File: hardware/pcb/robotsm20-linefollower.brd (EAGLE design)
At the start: 230 x 100 mm, 139 parts, among them Q5 BSS138LT3G, Q6 BSS138LT3G, Q7 BSS138LT3G, Q8 BSS138LT3G, SW1 CTS_219-4LPST, U1 STM32F405RG

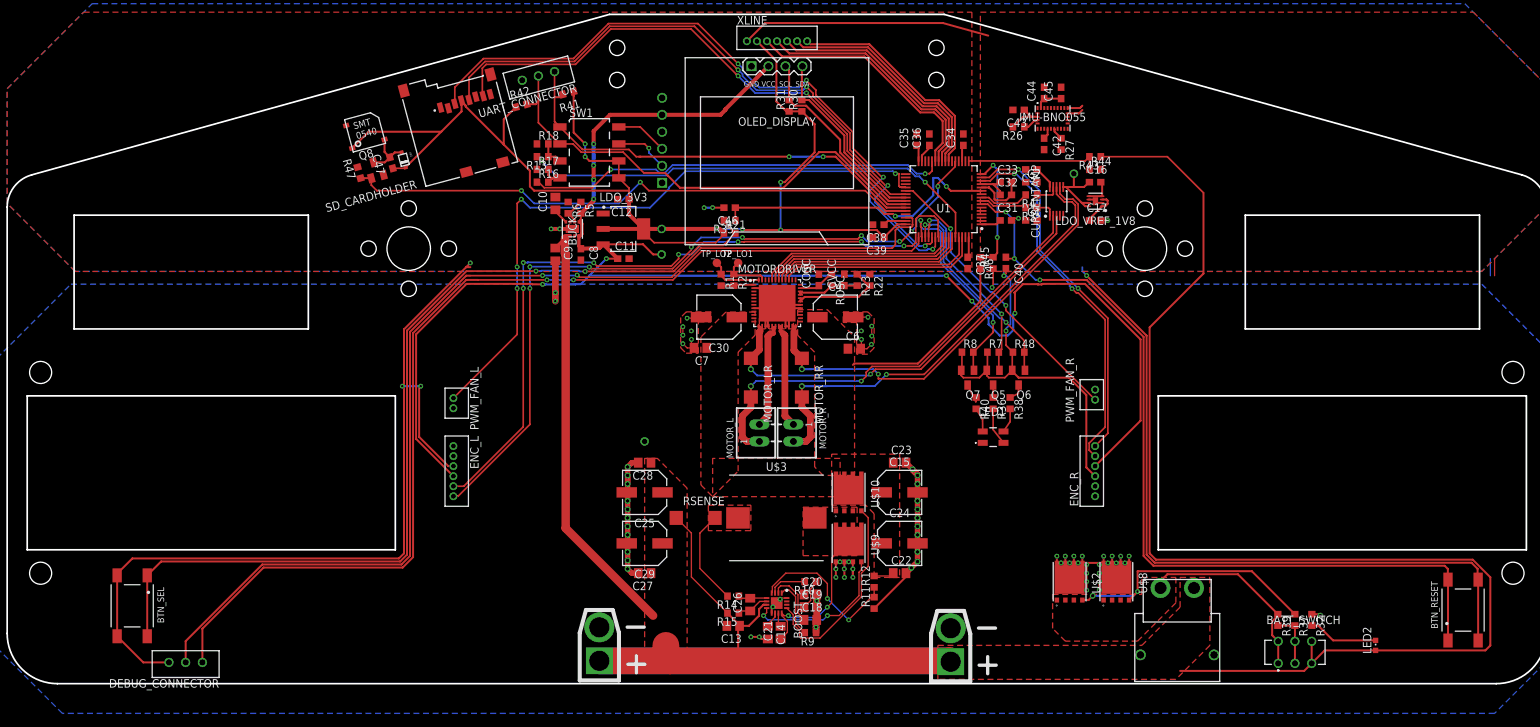
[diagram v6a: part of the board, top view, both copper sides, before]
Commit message: Moved around for battery
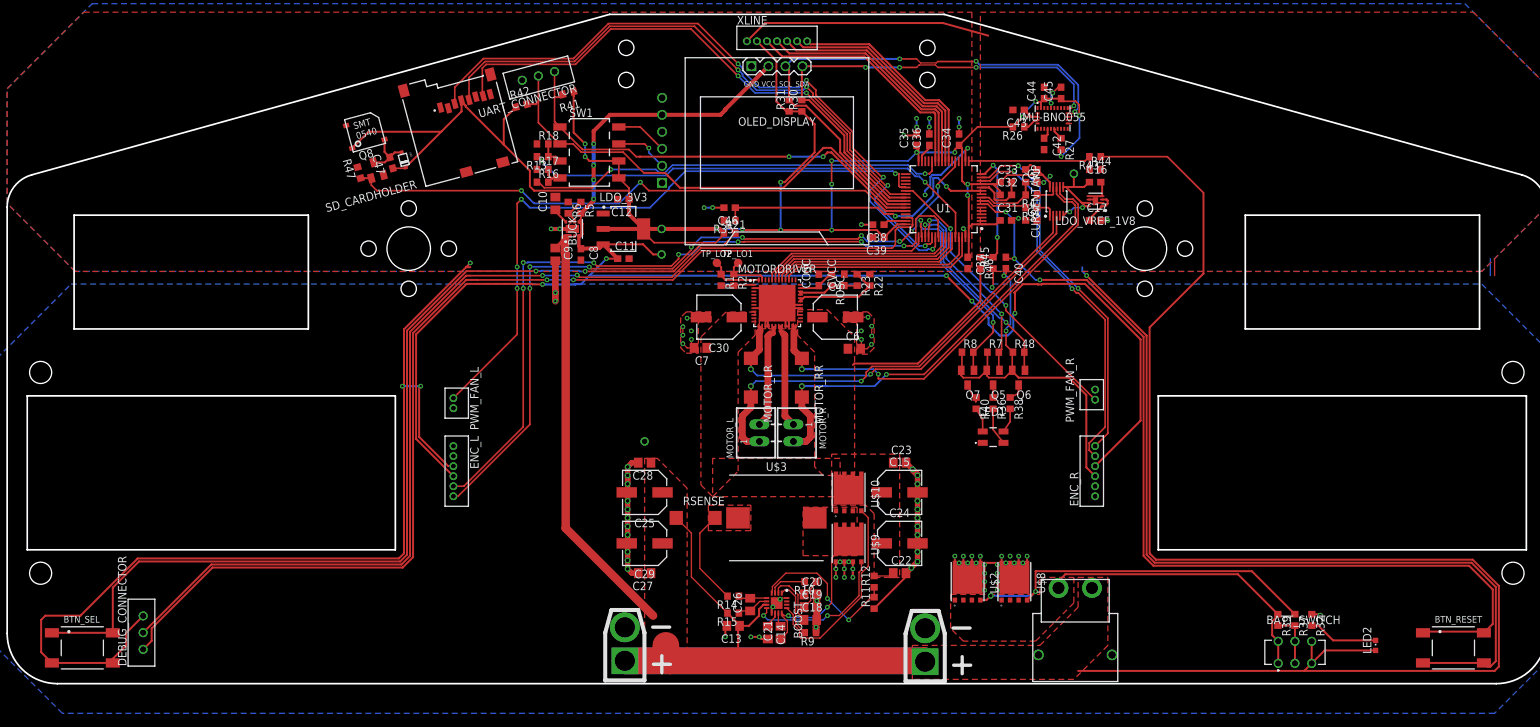
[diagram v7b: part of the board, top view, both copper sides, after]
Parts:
- moved U$15 15.2 mm to (159.6, 14.3)
- moved U$2 15.2 mm to (143.5, 15.2)
- moved U$8 15.2 mm to (150.5, 15.2)
- moved BTN_SEL 9.74 mm to (11.2, 5.35), turned to 0 degrees
- moved DEBUG_CONNECTOR 7.75 mm to (20.3, 7.62), turned to 90 degrees
- moved BTN_RESET 5.83 mm to (216.1, 5.35), turned to 0 degrees
- moved FAN_POWER_L 3.81 mm to (137.2, 3.28)
- moved FAN_POWER_R 3.81 mm to (92.3, 3.42)
- moved C34 0.63 mm to (142.2, 81.3)
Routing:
- net +3V3: track 231.8 -> 312.4 mm, vias 6 -> 17
- net DGND: track 307.0 -> 367.6 mm, vias 12 -> 23
- net SCL: track 32.5 -> 81.4 mm, vias 0 -> 3
- net SDA: track 30.5 -> 74.3 mm, vias 0 -> 4
- net V+: track 391.3 -> 406.9 mm
- net BAT-: track 29.5 -> 44.8 mm
- net N$41: track 39.8 -> 55.1 mm
- net !RESET: track 126.8 -> 140.5 mm
- net N$1: track 140.5 -> 153.1 mm
- net AGND: track 54.5 -> 64.1 mm, vias 0 -> 4
- net SWCLK: track 156.5 -> 162.7 mm
- net VREF: track 12.2 -> 16.6 mm, vias 0 -> 2
- net SWDIO: track 160.8 -> 163.5 mm
- net MOTOR_R_CUR: track 7.44 -> 9.35 mm
- net XLINE: track 37.7 -> 36.7 mm
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
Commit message: Finished all airwires
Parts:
- moved TP_12V 20.5 mm to (97.8, 56.5)
- moved R22 1.27 mm to (130.2, 60.3)
- moved R23 1.27 mm to (128.3, 60.3)
- moved CVCC 0.64 mm to (125.7, 60.3)
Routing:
- net +3V3: track 312.4 -> 359.2 mm, vias 17 -> 21
- net GND: track 144.9 -> 173.3 mm, vias 75 -> 82
- net VCC5V: track 14.4 -> 34.9 mm, vias 0 -> 2
- net +12V: track 30.9 -> 43.8 mm
- net DGND: track 367.6 -> 373.5 mm, vias 23 -> 27
- net AGND: track 64.1 -> 68.2 mm, vias 4 -> 7
- net MOTOR_L+_HIGH: track 64.6 -> 66.6 mm
- net MOTOR_L_CUR: track 7.00 -> 8.91 mm
- net N$28: track 14.5 -> 16.3 mm
- net N$19: track 23.5 -> 24.8 mm
- net PWM_FAN_R: track 43.7 -> 44.5 mm
- net VOLTM_BATT: track 20.2 -> 20.9 mm, vias 0 -> 2
- net N$31: track 5.52 -> 6.20 mm
- net ENC_L_A: track 113.3 -> 113.9 mm
- net MOTOR_R-: track 15.4 -> 15.9 mm
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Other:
- outline, holes or cut-outs redrawn
